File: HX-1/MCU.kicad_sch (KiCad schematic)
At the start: 33 parts, among them J10 Conn_01x24, J11 Conn_01x08, J12 USART_CONN, J3 I2C_CONN, J4 SPI_CONN, J7 FDCAN_CONN, J8 UART_CONN, J9 Conn_01x24, SW1 SW_SPDT, U1 STM32H723ZGT6

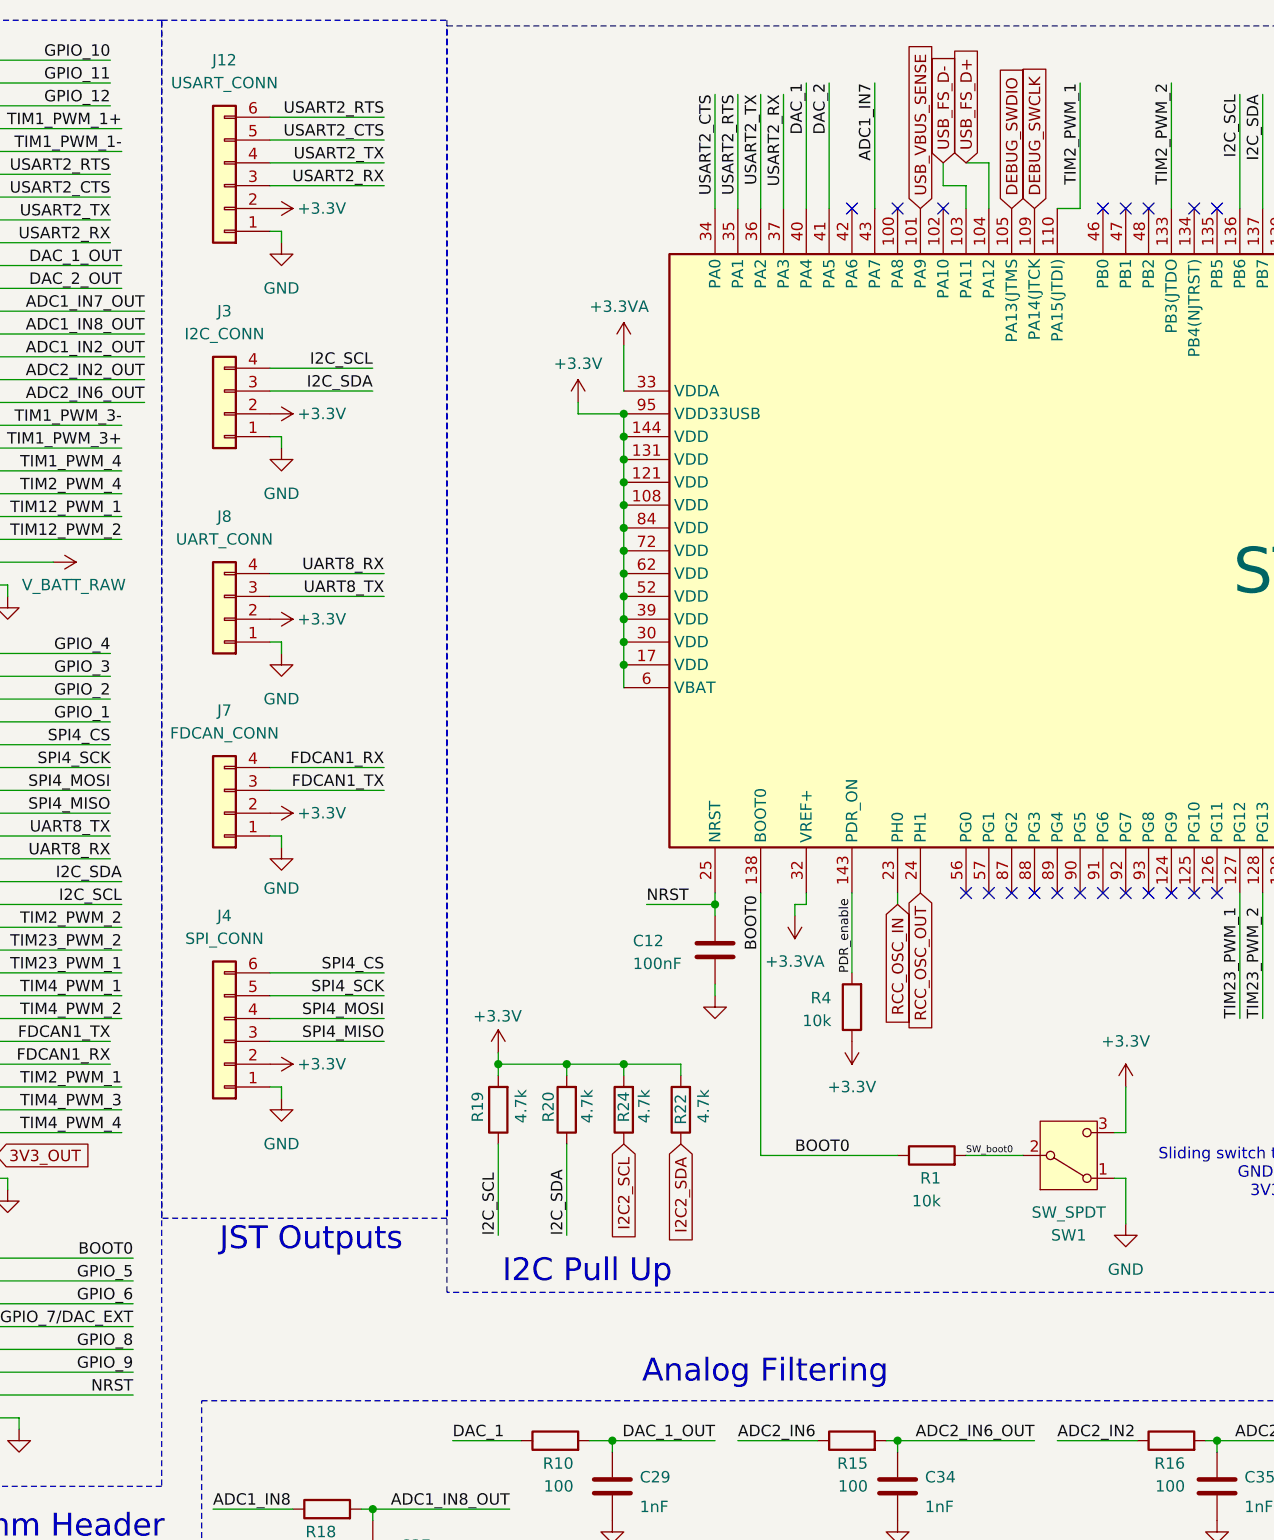
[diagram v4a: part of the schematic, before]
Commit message: remove fdcan connector for space, add header debug pin
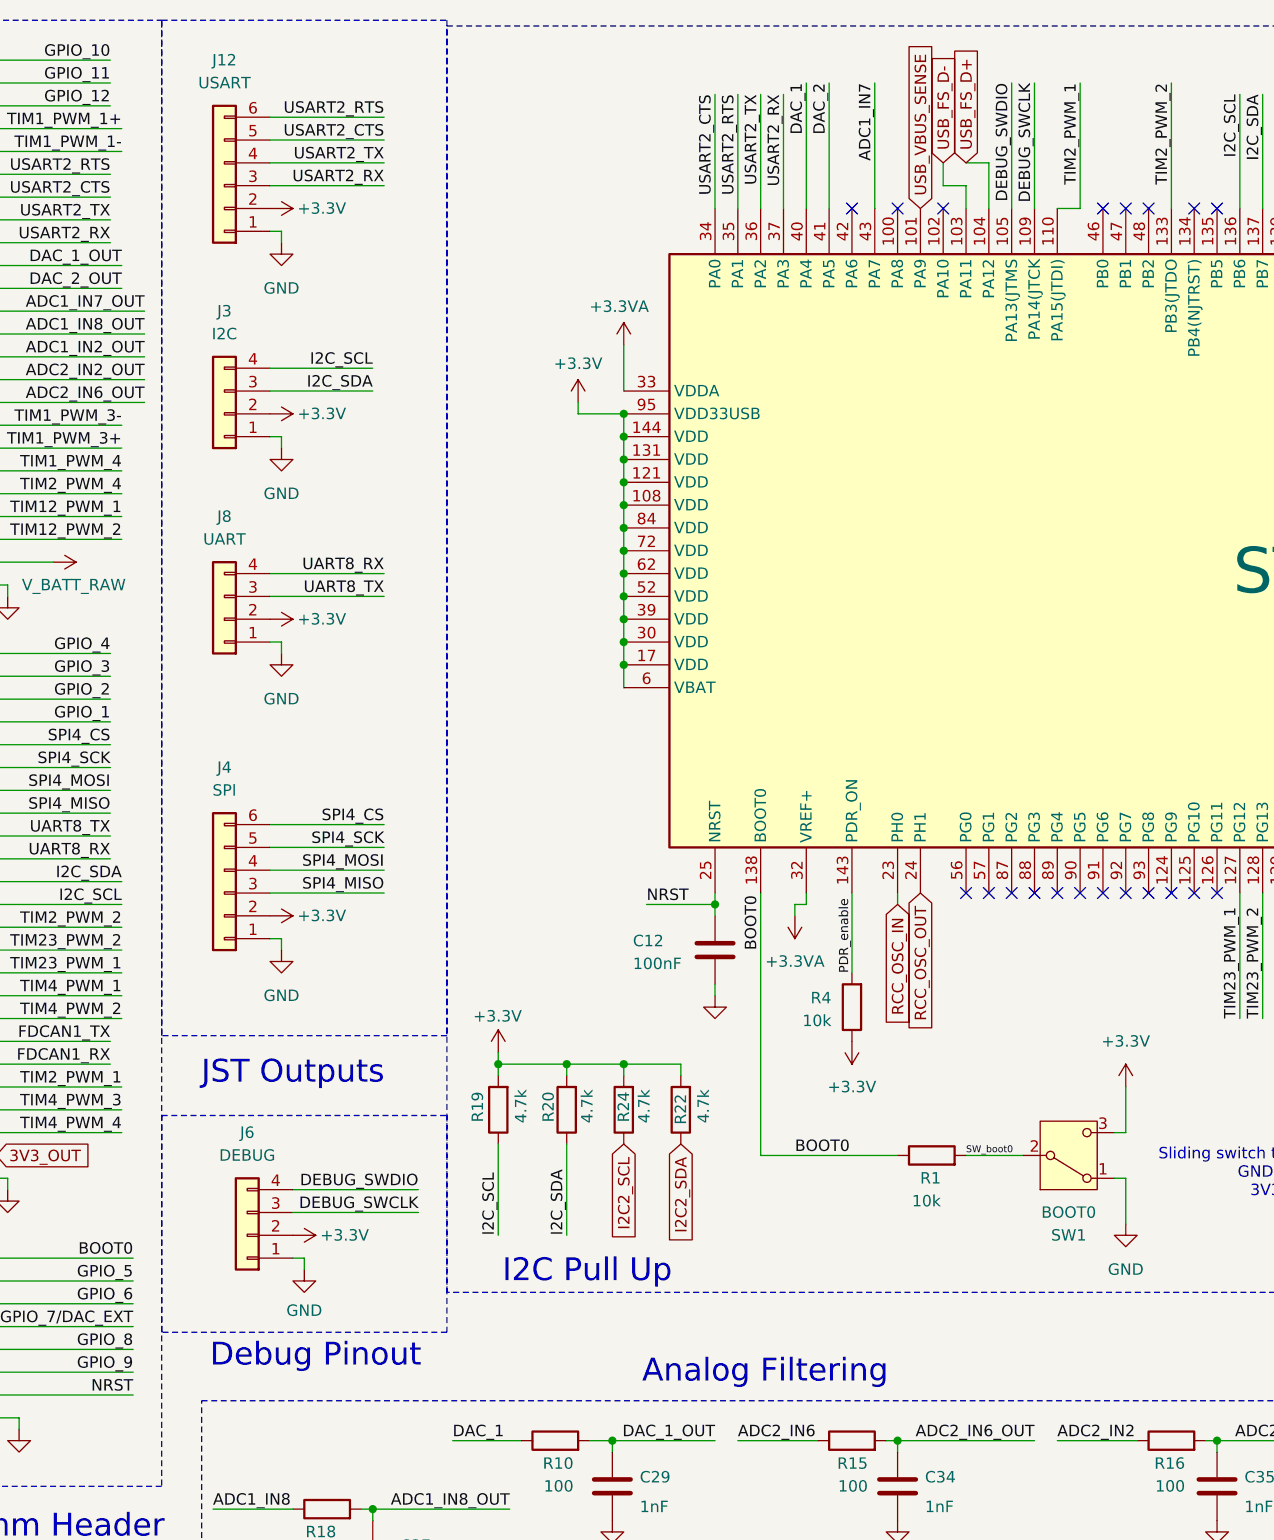
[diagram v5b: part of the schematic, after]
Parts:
- removed J7: FDCAN_CONN, Connector_JST:JST_PH_B4B-PH-K_1x04_P2.00mm_Vertical, symbol Connector_Generic:Conn_01x04
- added J6: DEBUG, Connector_PinHeader_2.54mm:PinHeader_1x04_P2.54mm_Vertical, symbol Connector_Generic:Conn_01x04
- J12: value USART_CONN -> USART
- J3: value I2C_CONN -> I2C
- J4: value SPI_CONN -> SPI
- J8: value UART_CONN -> UART
- SW1: value SW_SPDT -> BOOT0
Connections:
- net +3.3V: now also J6.2 (Pin_2)
- net DEBUG_SWCLK: now also J6.3 (Pin_3)
- net DEBUG_SWDIO: now also J6.4 (Pin_4)
- net GND: now also J6.1 (Pin_1)
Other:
- note added: "Debug Pinout"
- moved on the sheet: J4

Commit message: renumber capacitors, position all MCU caps
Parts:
- renumbered C12 to C28, C21 to C29, C24 to C30, C37 to C31, C29 to C32, C30 to C33, C32 to C35, C35 to C36, C36 to C37

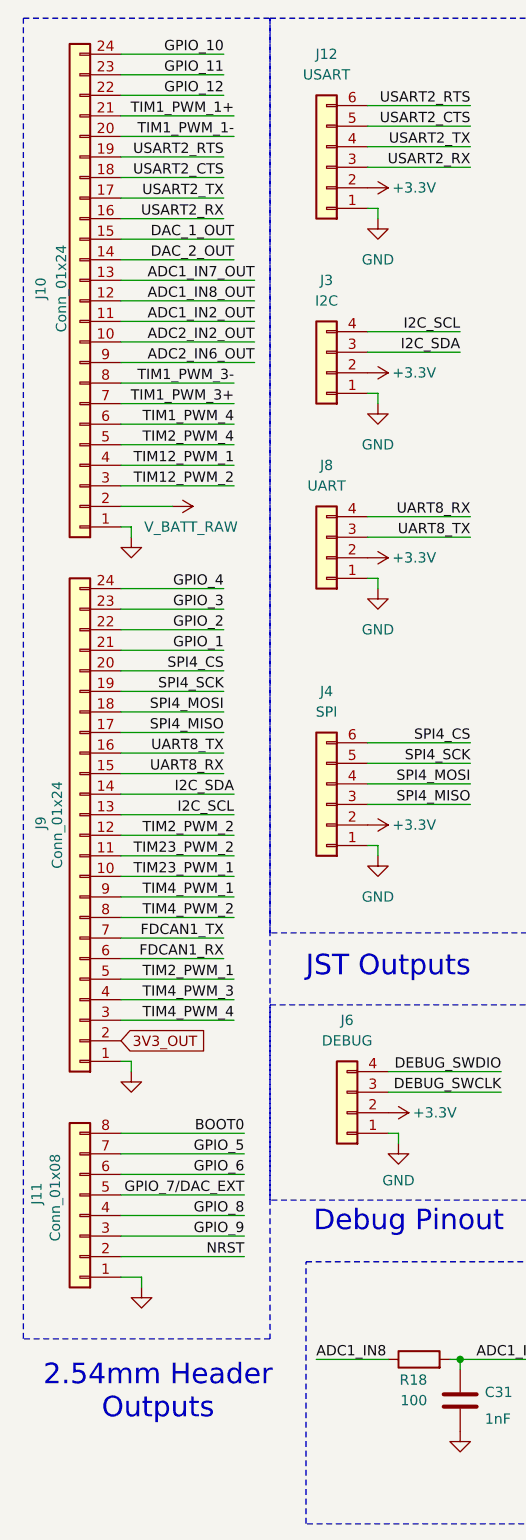
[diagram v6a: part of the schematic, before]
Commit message: remove 8 pin header on top of board, extend side headers by 4 each to replace pins
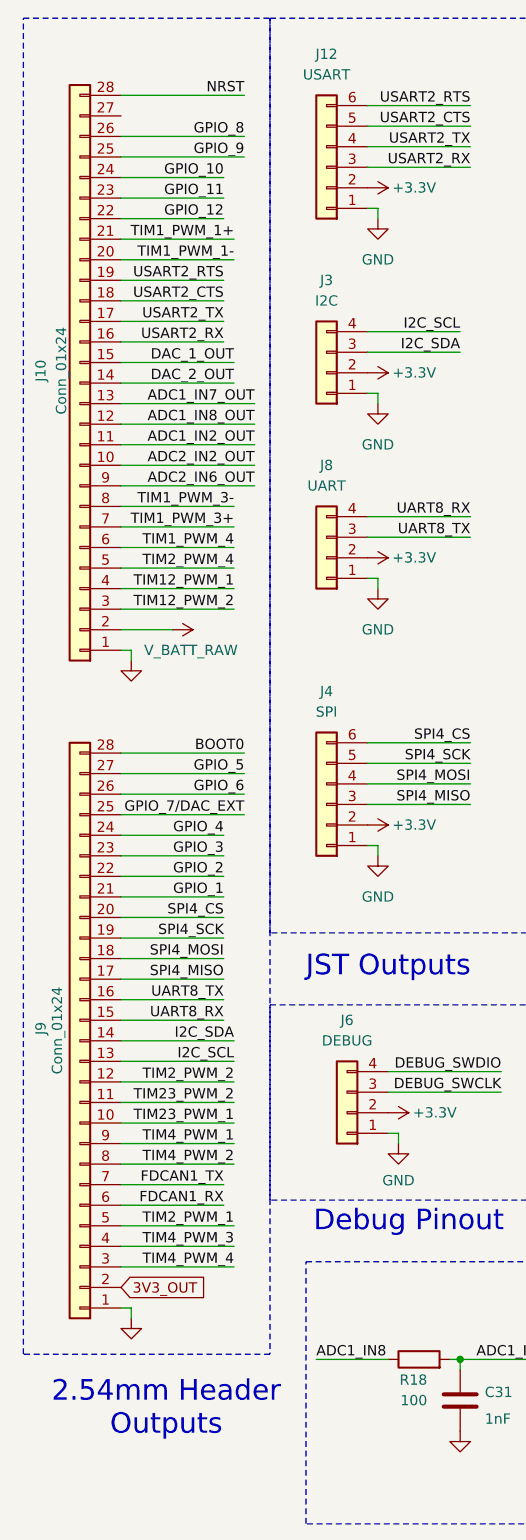
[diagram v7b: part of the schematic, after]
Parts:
- removed J11: Conn_01x08, Connector_PinHeader_2.54mm:PinHeader_1x08_P2.54mm_Vertical, symbol Connector_Generic:Conn_01x08
- J10, J9: footprint Connector_PinHeader_2.54mm:PinHeader_1x24_P2.54mm_Vertical -> Connector_PinHeader_2.54mm:PinHeader_1x28_P2.54mm_Vertical; symbol Connector_Generic:Conn_01x24 -> Connector_Generic:Conn_01x28
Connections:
- net BOOT0: now also J9.28 (Pin_28)
- net GPIO_5: now also J9.27 (Pin_27)
- net GPIO_6: now also J9.26 (Pin_26)
- net GPIO_7/DAC_EXT: now also J9.25 (Pin_25)
- net GPIO_8: now also J10.26 (Pin_26)
- net GPIO_9: now also J10.25 (Pin_25)
- net NRST: now also J10.28 (Pin_28)

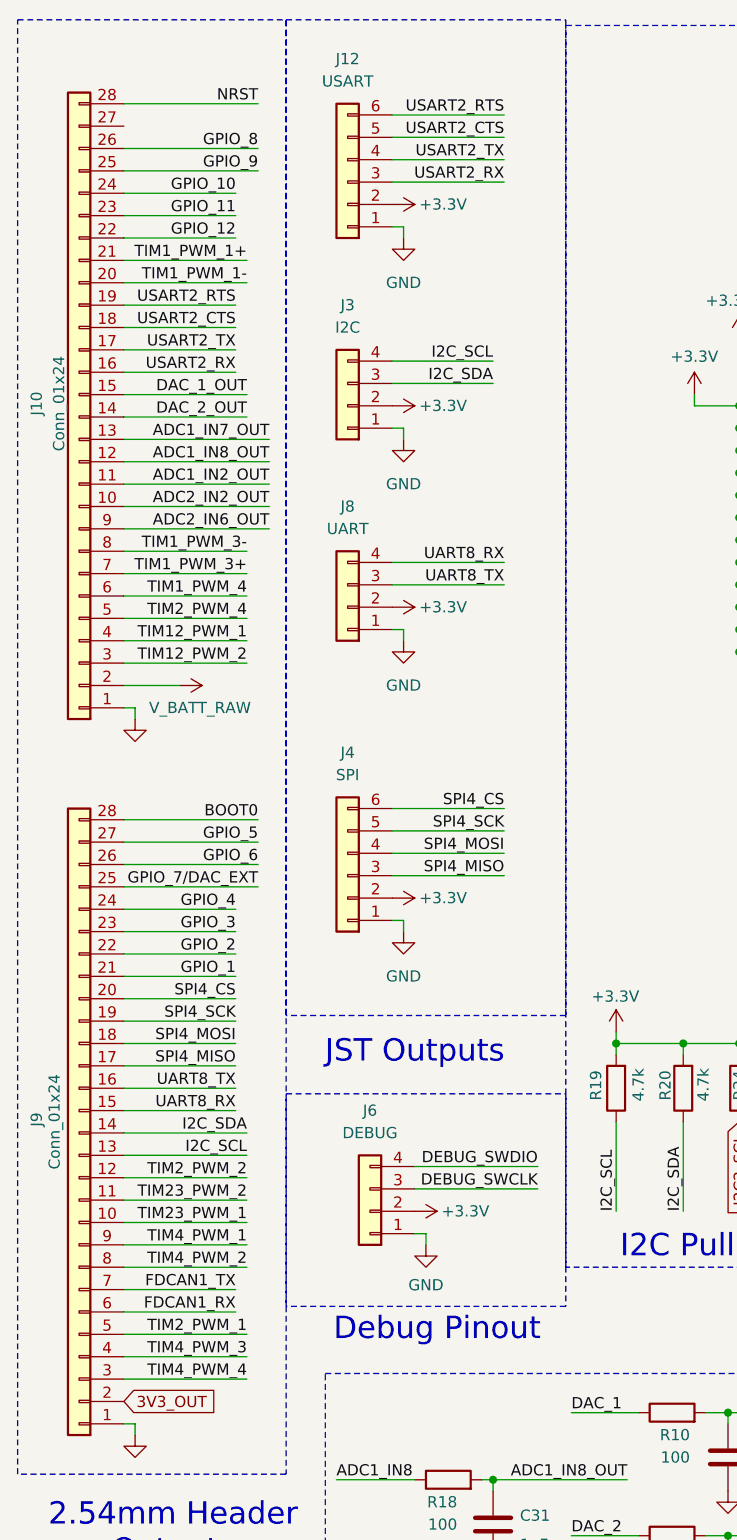
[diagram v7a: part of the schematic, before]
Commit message: remove GPIO 12 and DEBUG conn, add debug to right header
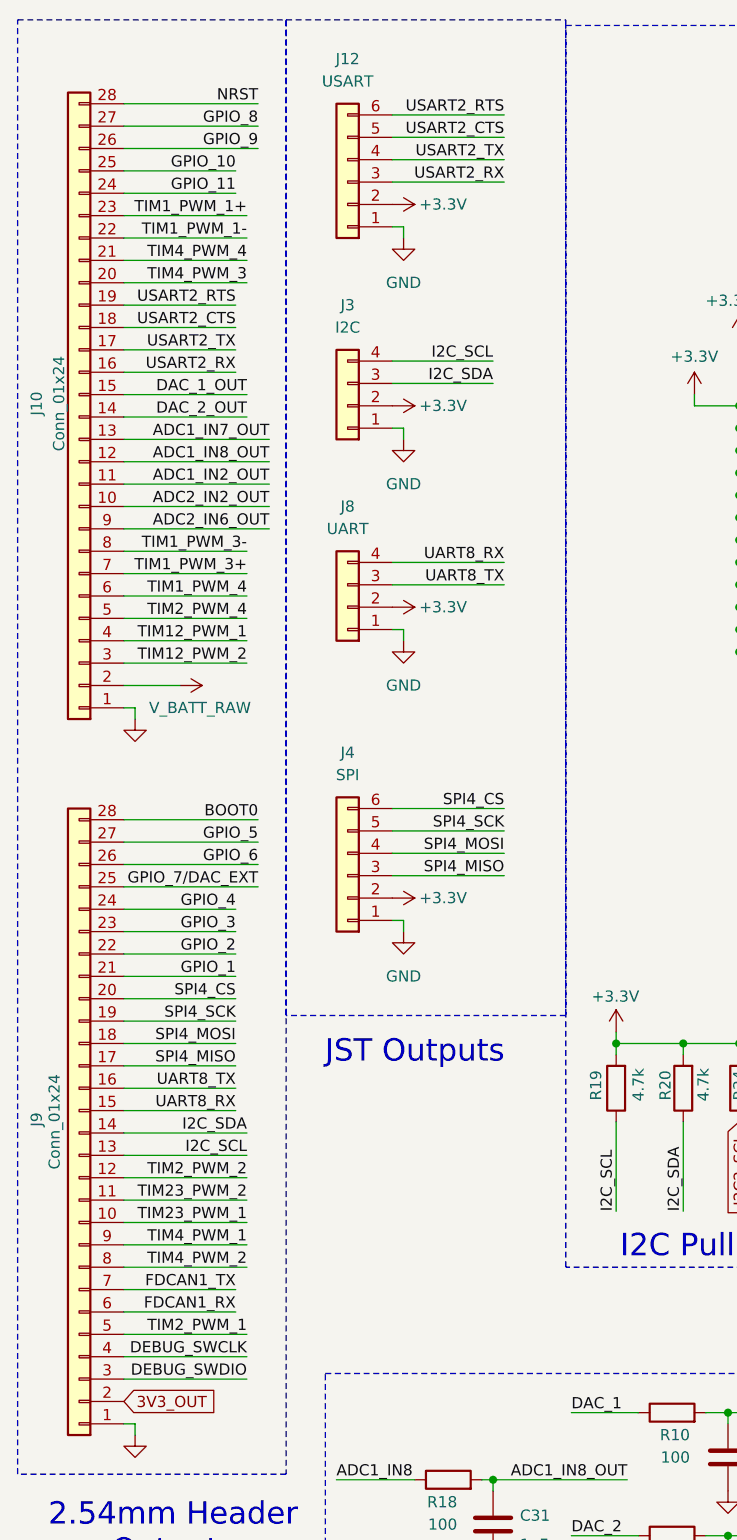
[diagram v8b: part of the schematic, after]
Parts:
- removed J6: DEBUG, Connector_PinHeader_2.54mm:PinHeader_1x04_P2.54mm_Vertical, symbol Connector_Generic:Conn_01x04
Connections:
- net DEBUG_SWCLK: now also J9.4 (Pin_4)
- net DEBUG_SWDIO: now also J9.3 (Pin_3)
- net GPIO_10: now also J10.25 (Pin_25); no longer J10.24 (Pin_24)
- net GPIO_11: now also J10.24 (Pin_24); no longer J10.23 (Pin_23)
- net GPIO_12: no longer J10.22 (Pin_22)
- net GPIO_8: now also J10.27 (Pin_27); no longer J10.26 (Pin_26)
- net GPIO_9: now also J10.26 (Pin_26); no longer J10.25 (Pin_25)
- net TIM1_PWM_1+: now also J10.23 (Pin_23); no longer J10.21 (Pin_21)
- net TIM1_PWM_1-: now also J10.22 (Pin_22); no longer J10.20 (Pin_20)
- net TIM4_PWM_3: now also J10.20 (Pin_20); no longer J9.4 (Pin_4)
- net TIM4_PWM_4: now also J10.21 (Pin_21); no longer J9.3 (Pin_3)
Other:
- note removed: "Debug Pinout"
